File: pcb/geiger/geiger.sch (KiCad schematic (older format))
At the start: 120 parts, among them J1 Conn_01x02, J2 Conn_01x02, J3 Conn_01x03, J4 Conn_01x06, J5 Conn_01x02, J6 Conn_02x05_Odd_Even, J7 Conn_02x05_Odd_Even, K1 RELAY_DPST, Q1 BC140, Q2 BC107, Q3 BC211, Q4 IRF540N, Q5 BC313, Q6 IRF540N, Q7 BC307, Q8 BC847, Q9 BC847, T1 Transformer_1P_1S, U1 MSP430G2553_PW20, U2 74HC595, U3 AD558, U4 MAA725, U5 LM2596, U6 MCP1402, X1 5.7MHz

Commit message: All connections ready.
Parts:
- added C39: 6u8, Capacitors_Tantalum_SMD:CP_Tantalum_Case-D_EIA-7343-31_Hand, symbol CP
- R41: footprint Resistors_ThroughHole:R_Axial_DIN0207_L6.3mm_D2.5mm_P10.16mm_Horizontal -> Resistors_ThroughHole:R_Axial_DIN0309_L9.0mm_D3.2mm_P12.70mm_Horizontal
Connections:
- net +36V: now also C39.1
- net GND: now also C39.2
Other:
- moved on the sheet: C31

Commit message: Add every feature on the board. Beta.
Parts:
- R42: footprint Resistors_ThroughHole:R_Axial_DIN0309_L9.0mm_D3.2mm_P12.70mm_Horizontal -> Resistors_ThroughHole:R_Axial_DIN0309_L9.0mm_D3.2mm_P15.24mm_Horizontal

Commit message: Final version of geiger board.
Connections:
- net GND: now also J4.5 (Pin_5), V1.4; no longer V1.3
- net HEATER_6_3V: now also V1.3; no longer V1.4
- no-connect marks 14 -> 13
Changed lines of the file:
@@
 	1    0    0    -1
 $EndComp
-Text GLabel 11700 2400 2    60   Input ~ 0
+Text GLabel 11700 2650 2    60   Input ~ 0
 HEATER_6_3V
-$Comp
-L GND #PWR085
-U 1 1 5AB7A67B
-P 11800 2600
-F 0 "#PWR085" H 11800 2350 50  0001 C CNN
-F 1 "GND" H 11800 2450 50  0000 C CNN
-F 2 "" H 11800 2600 50  0001 C CNN
-F 3 "" H 11800 2600 50  0001 C CNN
-	1    11800 2600
-	1    0    0    -1
-$EndComp
 $Comp
 L MCP1402 U6
@@
 $EndComp
 $Comp
-L GND #PWR086
+L GND #PWR085
 U 1 1 5ABD551A
 P 10700 6050
-F 0 "#PWR086" H 10700 5800 50  0001 C CNN
+F 0 "#PWR085" H 10700 5800 50  0001 C CNN
 F 1 "GND" H 10700 5900 50  0000 C CNN
 F 2 "" H 10700 6050 50  0001 C CNN
@@
 $EndComp
 $Comp
-L +15V #PWR087
+L +15V #PWR086
 U 1 1 5ABD6D23
 P 10500 5100
-F 0 "#PWR087" H 10500 4950 50  0001 C CNN
+F 0 "#PWR086" H 10500 4950 50  0001 C CNN
 F 1 "+15V" H 10500 5240 50  0000 C CNN
 F 2 "" H 10500 5100 50  0001 C CNN
@@
 $EndComp
 $Comp
-L GND #PWR088
+L GND #PWR087
 U 1 1 5ABDFD00
 P 9650 2900
-F 0 "#PWR088" H 9650 2650 50  0001 C CNN
+F 0 "#PWR087" H 9650 2650 50  0001 C CNN
 F 1 "GND" H 9650 2750 50  0000 C CNN
 F 2 "" H 9650 2900 50  0001 C CNN
@@
 $EndComp
 $Comp
-L GND #PWR089
+L GND #PWR088
 U 1 1 5ABE068E
 P 13850 2900
-F 0 "#PWR089" H 13850 2650 50  0001 C CNN
+F 0 "#PWR088" H 13850 2650 50  0001 C CNN
 F 1 "GND" H 13850 2750 50  0000 C CNN
 F 2 "" H 13850 2900 50  0001 C CNN
@@
 $EndComp
 $Comp
-L GND #PWR090
+L GND #PWR089
 U 1 1 5ABE2D0E
 P 10500 6050
-F 0 "#PWR090" H 10500 5800 50  0001 C CNN
+F 0 "#PWR089" H 10500 5800 50  0001 C CNN
 F 1 "GND" H 10500 5900 50  0000 C CNN
 F 2 "" H 10500 6050 50  0001 C CNN
@@
 $EndComp
 $Comp
-L PWR_FLAG #FLG091
+L PWR_FLAG #FLG090
 U 1 1 5ABE7925
 P 12250 1800
-F 0 "#FLG091" H 12250 1875 50  0001 C CNN
+F 0 "#FLG090" H 12250 1875 50  0001 C CNN
 F 1 "PWR_FLAG" H 12250 1950 50  0000 C CNN
 F 2 "" H 12250 1800 50  0001 C CNN
@@
 $EndComp
 $Comp
-L PWR_FLAG #FLG092
+L PWR_FLAG #FLG091
 U 1 1 5ABEA934
 P 9300 10100
-F 0 "#FLG092" H 9300 10175 50  0001 C CNN
+F 0 "#FLG091" H 9300 10175 50  0001 C CNN
 F 1 "PWR_FLAG" H 9300 10250 50  0000 C CNN
 F 2 "" H 9300 10100 50  0001 C CNN
@@
 $EndComp
 $Comp
-L PWR_FLAG #FLG093
+L PWR_FLAG #FLG092
 U 1 1 5ABEC7D5
 P 2150 1350
-F 0 "#FLG093" H 2150 1425 50  0001 C CNN
+F 0 "#FLG092" H 2150 1425 50  0001 C CNN
 F 1 "PWR_FLAG" H 2150 1500 50  0000 C CNN
 F 2 "" H 2150 1350 50  0001 C CNN
@@
 $EndComp
 $Comp
-L GND #PWR094
+L GND #PWR093
 U 1 1 5ABF4B7D
 P 15250 9050
-F 0 "#PWR094" H 15250 8800 50  0001 C CNN
+F 0 "#PWR093" H 15250 8800 50  0001 C CNN
 F 1 "GND" H 15250 8900 50  0000 C CNN
 F 2 "" H 15250 9050 50  0001 C CNN
@@
 $EndComp
 $Comp
-L GND #PWR095
+L GND #PWR094
 U 1 1 5ACAA398
 P 9250 1700
-F 0 "#PWR095" H 9250 1450 50  0001 C CNN
+F 0 "#PWR094" H 9250 1450 50  0001 C CNN
 F 1 "GND" H 9250 1550 50  0000 C CNN
 F 2 "" H 9250 1700 50  0001 C CNN
@@
 $EndComp
 $Comp
-L GND #PWR096
+L GND #PWR095
 U 1 1 5ACAA50B
 P 8950 1700
-F 0 "#PWR096" H 8950 1450 50  0001 C CNN
+F 0 "#PWR095" H 8950 1450 50  0001 C CNN
 F 1 "GND" H 8950 1550 50  0000 C CNN
 F 2 "" H 8950 1700 50  0001 C CNN
@@
 	2250 8600 2100 8600
 Wire Wire Line
-	15000 2100 15000 2900
+	15000 1800 15000 2900
 Wire Wire Line
 	15350 2100 15000 2100
@@
 	9350 2000 9300 2000
 Wire Wire Line
-	10400 1300 10400 1350
+	10400 1350 10400 1300
 Wire Wire Line
 	9950 1400 9950 1350
@@
 	12550 2500 12550 2900
 Wire Wire Line
-	11700 2400 11550 2400
-Wire Wire Line
-	11550 2500 11800 2500
-Wire Wire Line
-	11800 2500 11800 2600
-Wire Wire Line
 	12550 1900 12550 2200
 Wire Wire Line
@@
 	2250 8500 2100 8500
 $Comp
-L +3.3V #PWR097
+L +3.3V #PWR096
 U 1 1 5ACBBC67
 P 14450 2900
-F 0 "#PWR097" H 14450 2750 50  0001 C CNN
+F 0 "#PWR096" H 14450 2750 50  0001 C CNN
 F 1 "+3.3V" H 14450 3040 50  0000 C CNN
 F 2 "" H 14450 2900 50  0001 C CNN
@@
 Connection ~ 11900 1750
 $Comp
-L GND #PWR098
+L GND #PWR097
 U 1 1 5ACC1F6D
 P 11300 1400
-F 0 "#PWR098" H 11300 1150 50  0001 C CNN
+F 0 "#PWR097" H 11300 1150 50  0001 C CNN
 F 1 "GND" H 11300 1250 50  0000 C CNN
 F 2 "" H 11300 1400 50  0001 C CNN
@@
 Wire Wire Line
 	15350 1700 15250 1700
-NoConn ~ 15350 1800
 NoConn ~ 2250 8400
 NoConn ~ 6150 8400
@@
 $EndComp
 $Comp
-L GND #PWR099
+L GND #PWR098
 U 1 1 5ACD3AB5
 P 10200 1700
-F 0 "#PWR099" H 10200 1450 50  0001 C CNN
+F 0 "#PWR098" H 10200 1450 50  0001 C CNN
 F 1 "GND" H 10200 1550 50  0000 C CNN
 F 2 "" H 10200 1700 50  0001 C CNN
@@
 	10200 1400 10200 1350
 Connection ~ 10200 1350
+Wire Wire Line
+	15350 1800 15000 1800
+Connection ~ 15000 2100
+Wire Wire Line
+	11550 2400 12100 2400
+Wire Wire Line
+	12100 2400 12100 2550
+Wire Wire Line
+	12100 2550 12550 2550
+Connection ~ 12550 2550
+Wire Wire Line
+	11700 2650 11650 2650
+Wire Wire Line
+	11650 2650 11650 2500
+Wire Wire Line
+	11650 2500 11550 2500
 $EndSCHEMATC

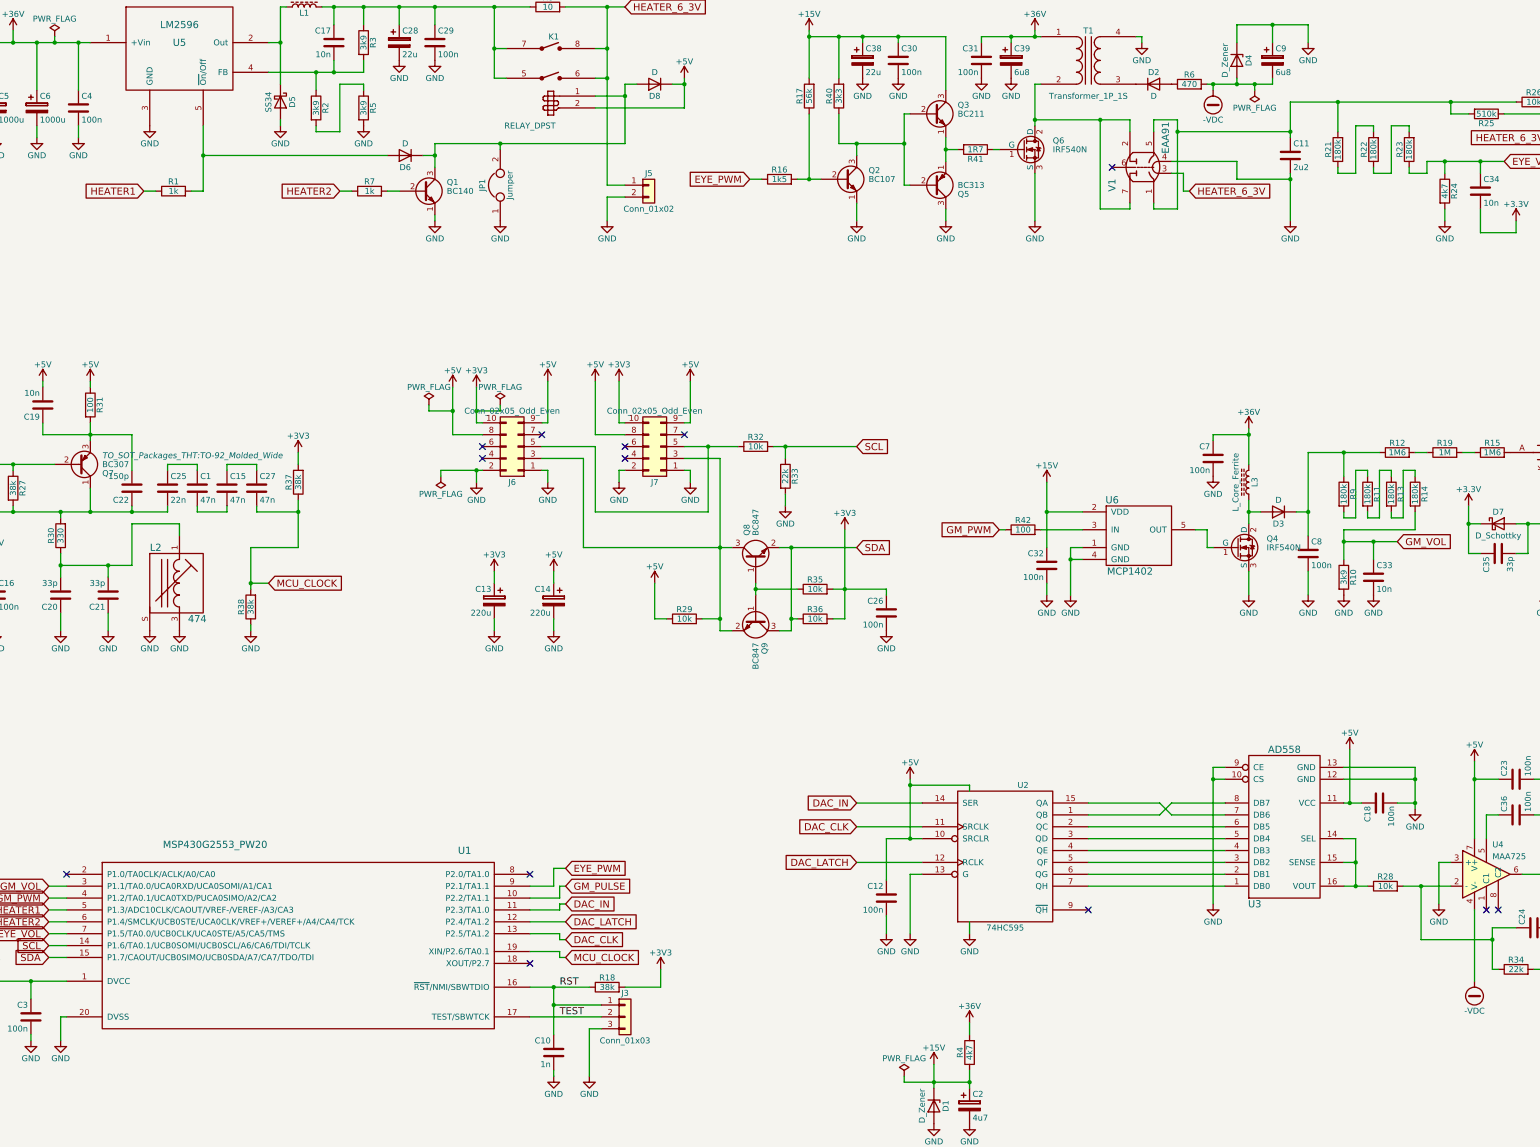
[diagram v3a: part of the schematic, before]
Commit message: Change some element values geiger.
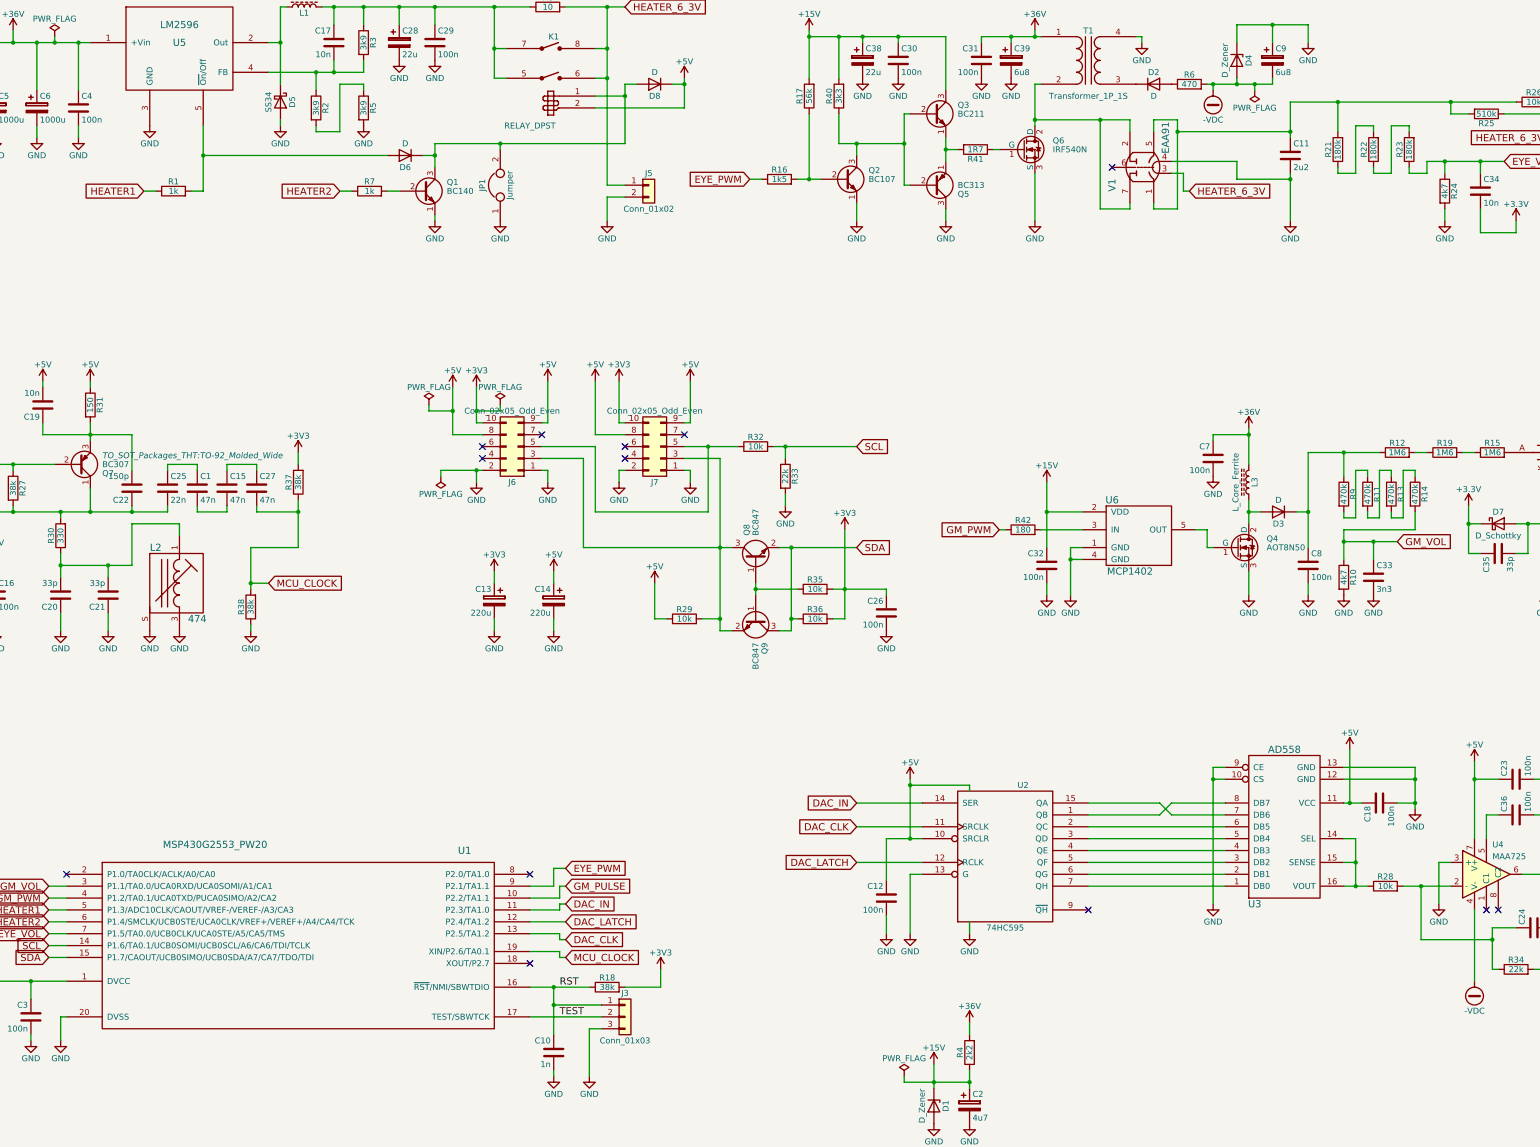
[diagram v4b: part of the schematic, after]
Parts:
- C33: value 10n -> 3n3
- Q4: value IRF540N -> AOT8N50
- R10: value 3k9 -> 4k7
- R11, R13, R14, R9: value 180k -> 470k
- R19: value 1M -> 1M6
- R31: value 100 -> 150
- R4: value 4k7 -> 2k2
- R42: value 100 -> 180
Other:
- moved on the sheet: C8
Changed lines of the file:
@@
 P 2450 4450
 F 0 "R31" V 2530 4450 50  0000 C CNN
-F 1 "100" V 2450 4450 50  0000 C CNN
+F 1 "150" V 2450 4450 50  0000 C CNN
 F 2 "Resistors_ThroughHole:R_Axial_DIN0207_L6.3mm_D2.5mm_P10.16mm_Horizontal" V 2380 4450 50  0001 C CNN
 F 3 "" H 2450 4450 50  0000 C CNN
@@
 P 12100 5650
 F 0 "Q4" H 12350 5725 50  0000 L CNN
-F 1 "IRF540N" H 12350 5650 50  0000 L CNN
+F 1 "AOT8N50" H 12350 5650 50  0000 L CNN
 F 2 "TO_SOT_Packages_THT:TO-220-3_Vertical" H 12350 5575 50  0001 L CIN
 F 3 "" H 12100 5650 50  0001 L CNN
@@
 L C C8
 U 1 1 59E91D39
-P 12700 5700
-F 0 "C8" H 12725 5800 50  0000 L CNN
-F 1 "100n" H 12725 5600 50  0000 L CNN
-F 2 "Capacitors_ThroughHole:C_Rect_L33.0mm_W13.0mm_P27.50mm_MKS4" H 12738 5550 50  0001 C CNN
-F 3 "" H 12700 5700 50  0000 C CNN
-	1    12700 5700
+P 12700 5800
+F 0 "C8" H 12725 5900 50  0000 L CNN
+F 1 "100n" H 12725 5700 50  0000 L CNN
+F 2 "Capacitors_ThroughHole:C_Rect_L33.0mm_W13.0mm_P27.50mm_MKS4" H 12738 5650 50  0001 C CNN
+F 3 "" H 12700 5800 50  0000 C CNN
+	1    12700 5800
 	1    0    0    -1
 $EndComp
@@
 P 13000 5200
 F 0 "R9" V 13080 5200 50  0000 C CNN
-F 1 "180k" V 13000 5200 50  0000 C CNN
+F 1 "470k" V 13000 5200 50  0000 C CNN
 F 2 "Resistors_SMD:R_1206_HandSoldering" V 12930 5200 50  0001 C CNN
 F 3 "" H 13000 5200 50  0001 C CNN
@@
 P 13000 5900
 F 0 "R10" V 13080 5900 50  0000 C CNN
-F 1 "3k9" V 13000 5900 50  0000 C CNN
+F 1 "4k7" V 13000 5900 50  0000 C CNN
 F 2 "Resistors_SMD:R_1206_HandSoldering" V 12930 5900 50  0001 C CNN
 F 3 "" H 13000 5900 50  0001 C CNN
@@
 P 13200 5200
 F 0 "R11" V 13280 5200 50  0000 C CNN
-F 1 "180k" V 13200 5200 50  0000 C CNN
+F 1 "470k" V 13200 5200 50  0000 C CNN
 F 2 "Resistors_SMD:R_1206_HandSoldering" V 13130 5200 50  0001 C CNN
 F 3 "" H 13200 5200 50  0001 C CNN
@@
 P 9850 9900
 F 0 "R4" V 9930 9900 50  0000 C CNN
-F 1 "4k7" V 9850 9900 50  0000 C CNN
+F 1 "2k2" V 9850 9900 50  0000 C CNN
 F 2 "Resistors_ThroughHole:R_Axial_DIN0207_L6.3mm_D2.5mm_P10.16mm_Horizontal" V 9780 9900 50  0001 C CNN
 F 3 "" H 9850 9900 50  0001 C CNN
@@
 P 13400 5200
 F 0 "R13" V 13480 5200 50  0000 C CNN
-F 1 "180k" V 13400 5200 50  0000 C CNN
+F 1 "470k" V 13400 5200 50  0000 C CNN
 F 2 "Resistors_SMD:R_1206_HandSoldering" V 13330 5200 50  0001 C CNN
 F 3 "" H 13400 5200 50  0001 C CNN
@@
 P 13600 5200
 F 0 "R14" V 13680 5200 50  0000 C CNN
-F 1 "180k" V 13600 5200 50  0000 C CNN
+F 1 "470k" V 13600 5200 50  0000 C CNN
 F 2 "Resistors_SMD:R_1206_HandSoldering" V 13530 5200 50  0001 C CNN
 F 3 "" H 13600 5200 50  0001 C CNN
@@
 P 13850 4850
 F 0 "R19" V 13930 4850 50  0000 C CNN
-F 1 "1M" V 13850 4850 50  0000 C CNN
+F 1 "1M6" V 13850 4850 50  0000 C CNN
 F 2 "Resistors_ThroughHole:R_Axial_DIN0309_L9.0mm_D3.2mm_P12.70mm_Horizontal" V 13780 4850 50  0001 C CNN
 F 3 "" H 13850 4850 50  0001 C CNN
@@
 P 13250 5900
 F 0 "C33" H 13275 6000 50  0000 L CNN
-F 1 "10n" H 13275 5800 50  0000 L CNN
+F 1 "3n3" H 13275 5800 50  0000 L CNN
 F 2 "Capacitors_SMD:C_1206_HandSoldering" H 13288 5750 50  0001 C CNN
 F 3 "" H 13250 5900 50  0000 C CNN
@@
 P 10300 5500
 F 0 "R42" V 10380 5500 50  0000 C CNN
-F 1 "100" V 10300 5500 50  0000 C CNN
+F 1 "180" V 10300 5500 50  0000 C CNN
 F 2 "Resistors_ThroughHole:R_Axial_DIN0309_L9.0mm_D3.2mm_P15.24mm_Horizontal" V 10230 5500 50  0001 C CNN
 F 3 "" H 10300 5500 50  0001 C CNN
@@
 Connection ~ 13000 4850
 Wire Wire Line
-	12700 5850 12700 6050
+	12700 5950 12700 6050
 Wire Wire Line
 	12700 4850 13300 4850
 Wire Wire Line
-	12700 4850 12700 5550
+	12700 4850 12700 5650
 Wire Wire Line
 	12200 5850 12200 6050
@@
 	7050 1750 6950 1750
 Wire Wire Line
-	6950 1750 6950 2250
+	6950 2250 6950 1750
 Wire Wire Line
 	6950 1850 6700 1850
 Wire Wire Line
-	6950 2250 5350 2250
+	5350 2250 6950 2250
 Connection ~ 6950 1850
 Connection ~ 5900 2250
